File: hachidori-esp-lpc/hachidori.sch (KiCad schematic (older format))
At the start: 53 parts, among them P1 VIN, P2 UART, P3 ADC, P4 I2C, SW1 FLASH, SW2 RESET, U1 NCP1117ST33, U2 MPU-9250, U3 ESP-13-WROOM-02, U4 BME280, U7 INA226

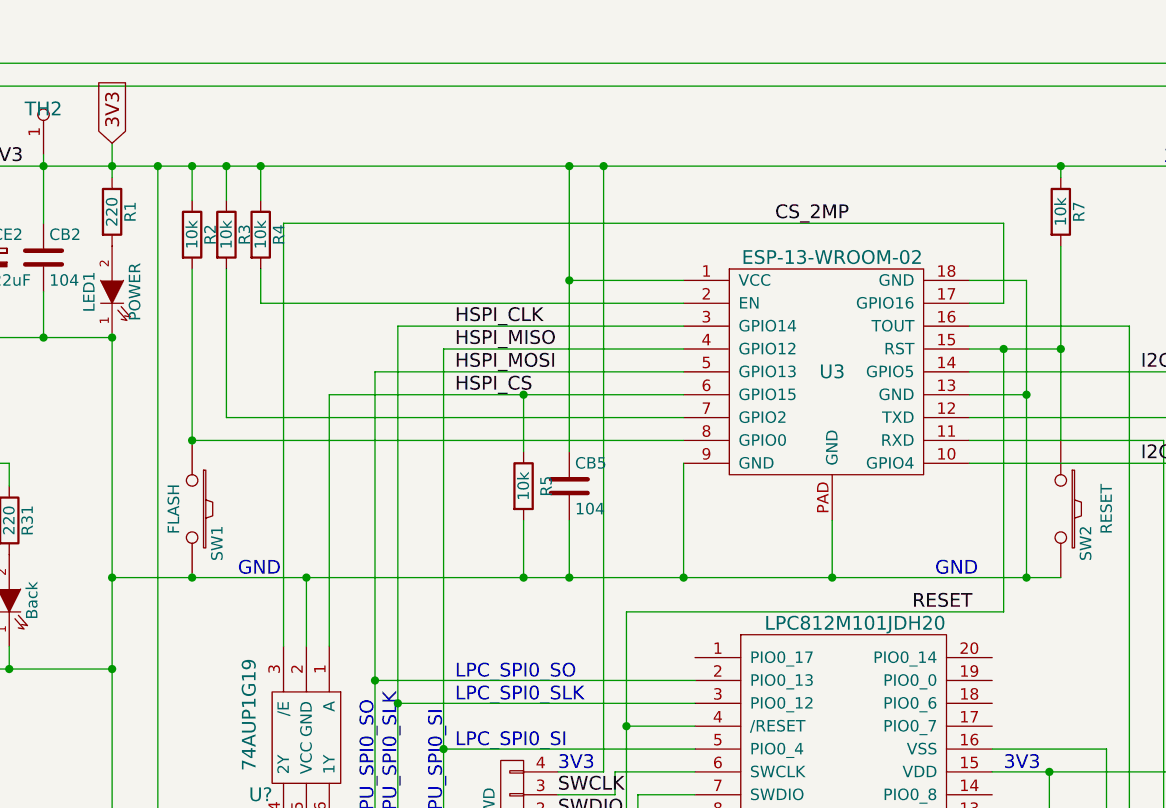
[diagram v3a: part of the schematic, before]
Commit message: Chang GPIO16 to GPIO2
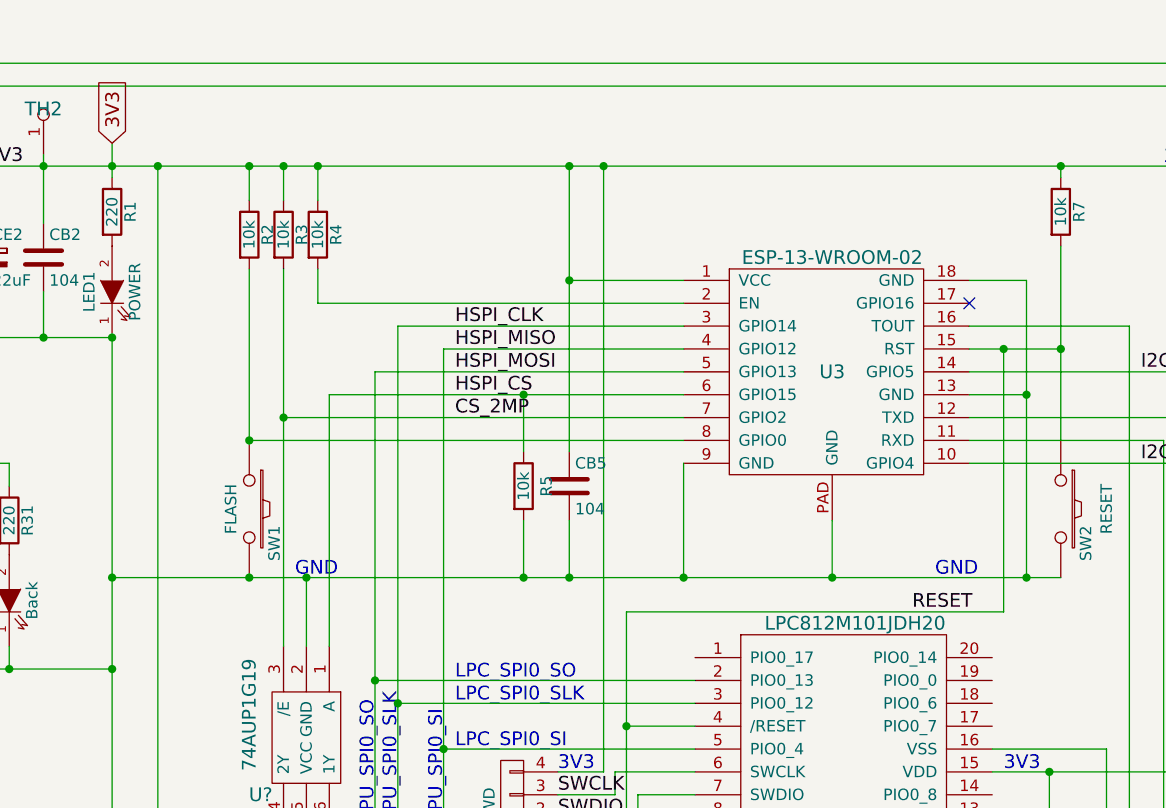
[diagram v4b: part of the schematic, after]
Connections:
- net CS_2MP: now also R3.2, U3.7 (GPIO2); no longer U3.17 (GPIO16)
- no-connect marks 5 -> 6
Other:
- moved on the sheet: R2, R3, R4, SW1
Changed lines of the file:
@@
 Title "hachidori-esp-lpc"
 Date "2017-02-12"
-Rev "0.04"
+Rev "0.05"
 Comp ""
 Comment1 "Copyright (c) 2016 DroneWorks Inc."
@@
 L R R4
 U 1 1 57B2B6BF
-P 3300 1550
-F 0 "R4" V 3380 1550 50  0000 C CNN
-F 1 "10k" V 3300 1550 50  0000 C CNN
-F 2 "rohm:MCR03" V 3230 1550 50  0001 C CNN
-F 3 "" H 3300 1550 50  0000 C CNN
-	1    3300 1550
+P 3550 1550
+F 0 "R4" V 3630 1550 50  0000 C CNN
+F 1 "10k" V 3550 1550 50  0000 C CNN
+F 2 "rohm:MCR03" V 3480 1550 50  0001 C CNN
+F 3 "" H 3550 1550 50  0000 C CNN
+	1    3550 1550
 	1    0    0    -1
 $EndComp
@@
 L R R3
 U 1 1 57B2C559
-P 3150 1550
-F 0 "R3" V 3230 1550 50  0000 C CNN
-F 1 "10k" V 3150 1550 50  0000 C CNN
-F 2 "rohm:MCR03" V 3080 1550 50  0001 C CNN
-F 3 "" H 3150 1550 50  0000 C CNN
-	1    3150 1550
+P 3400 1550
+F 0 "R3" V 3480 1550 50  0000 C CNN
+F 1 "10k" V 3400 1550 50  0000 C CNN
+F 2 "rohm:MCR03" V 3330 1550 50  0001 C CNN
+F 3 "" H 3400 1550 50  0000 C CNN
+	1    3400 1550
 	1    0    0    -1
 $EndComp
@@
 L R R2
 U 1 1 57B2C582
-P 3000 1550
-F 0 "R2" V 3080 1550 50  0000 C CNN
-F 1 "10k" V 3000 1550 50  0000 C CNN
-F 2 "rohm:MCR03" V 2930 1550 50  0001 C CNN
-F 3 "" H 3000 1550 50  0000 C CNN
-	1    3000 1550
+P 3250 1550
+F 0 "R2" V 3330 1550 50  0000 C CNN
+F 1 "10k" V 3250 1550 50  0000 C CNN
+F 2 "rohm:MCR03" V 3180 1550 50  0001 C CNN
+F 3 "" H 3250 1550 50  0000 C CNN
+	1    3250 1550
 	1    0    0    -1
 $EndComp
@@
 L SW_PUSH SW1
 U 1 1 57BD416E
-P 3000 2750
-F 0 "SW1" H 3150 2860 50  0000 C CNN
-F 1 "FLASH" H 3000 2670 50  0000 C CNN
-F 2 "droneworks:B3U-1000P" H 3000 2750 50  0001 C CNN
-F 3 "" H 3000 2750 50  0000 C CNN
-	1    3000 2750
+P 3250 2750
+F 0 "SW1" H 3400 2860 50  0000 C CNN
+F 1 "FLASH" H 3250 2670 50  0000 C CNN
+F 2 "droneworks:B3U-1000P" H 3250 2750 50  0001 C CNN
+F 3 "" H 3250 2750 50  0000 C CNN
+	1    3250 2750
 	0    1    1    0
 $EndComp
@@
 Text Notes 2900 4200 0    60   ~ 0
 3V3
-Text Notes 3200 3050 0    60   ~ 0
+Text Notes 3450 3050 0    60   ~ 0
 GND
 Text Label 3400 4450 0    60   ~ 0
@@
 Text Notes 6400 5400 0    60   ~ 0
 ESP-RXDpin
-Text Label 5550 1500 0    60   ~ 0
+Text Label 4150 2350 0    60   ~ 0
 CS_2MP
 $Comp
@@
 	-1   0    0    1
 $EndComp
+Text Label 4600 4100 0    60   ~ 0
+SWDIO
+Text Label 4600 4000 0    60   ~ 0
+SWCLK
+Text Notes 4600 4200 0    60   ~ 0
+GND
+Text Notes 4600 3900 0    60   ~ 0
+3V3
+NoConn ~ 6400 1850
 Wire Wire Line
 	2650 6500 10350 6500
@@
 Connection ~ 6650 3050
 Connection ~ 6800 2050
-Connection ~ 3000 2450
+Connection ~ 3250 2450
 Connection ~ 4450 3050
 Connection ~ 5300 6500
@@
 	2850 5000 3300 5000
 Wire Wire Line
-	3000 1700 3000 2450
-Connection ~ 3150 1250
-Wire Wire Line
-	3150 1250 3150 1400
-Connection ~ 3000 1250
-Wire Wire Line
-	3000 1250 3000 1400
-Wire Wire Line
-	3000 2450 5150 2450
-Wire Wire Line
-	3150 2350 3150 1700
-Wire Wire Line
-	5150 2350 3150 2350
+	3250 1700 3250 2450
+Connection ~ 3400 1250
+Wire Wire Line
+	3400 1250 3400 1400
+Connection ~ 3250 1250
+Wire Wire Line
+	3250 1250 3250 1400
+Wire Wire Line
+	3250 2450 5150 2450
+Wire Wire Line
+	3400 1700 3400 3350
+Wire Wire Line
+	5150 2350 3400 2350
 Wire Wire Line
 	4100 2050 5150 2050
@@
 	3800 2150 5150 2150
 Wire Wire Line
-	3300 1250 3300 1400
+	3550 1250 3550 1400
 Connection ~ 4650 1250
 Wire Wire Line
@@
 Wire Wire Line
 	10050 1250 10050 2450
-Connection ~ 3300 1250
+Connection ~ 3550 1250
 Connection ~ 1050 1250
 Connection ~ 2650 2000
@@
 Connection ~ 4000 6500
 Connection ~ 2650 3050
-Connection ~ 3000 3050
+Connection ~ 3250 3050
 Wire Wire Line
 	7650 1700 7650 3800
@@
 Connection ~ 3500 3050
 Wire Wire Line
-	5150 1850 3300 1850
-Wire Wire Line
-	3300 1850 3300 1700
-Wire Wire Line
-	6400 1850 6550 1850
-Wire Wire Line
-	6550 1850 6550 1500
-Wire Wire Line
-	3400 3350 3400 1500
-Wire Wire Line
-	3400 1500 6550 1500
+	5150 1850 3550 1850
+Wire Wire Line
+	3550 1850 3550 1700
 Wire Wire Line
 	2650 4600 3200 4600
@@
 Connection ~ 4800 1250
 Connection ~ 7550 3900
-Text Label 4600 4100 0    60   ~ 0
-SWDIO
-Text Label 4600 4000 0    60   ~ 0
-SWCLK
-Text Notes 4600 4200 0    60   ~ 0
-GND
-Text Notes 4600 3900 0    60   ~ 0
-3V3
+Connection ~ 3400 2350
 $EndSCHEMATC
